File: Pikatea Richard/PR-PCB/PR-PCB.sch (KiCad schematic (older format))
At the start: 7 parts, among them SW1 Rotary_Encoder_Switch, SW2 Rotary_Encoder_Switch

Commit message: updated footprints added gerbers
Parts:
- added U1: ProMicro, promicro:ProMicro, symbol promicro:ProMicro
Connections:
- net at MX2.1 (COL): now also MX1.1 (COL), MX3.1 (COL), MX4.1 (COL), MX5.1 (COL), U1.17 (F7)
- net at MX2.2 (ROW): now also U1.11 (B4)
- net at MX3.2 (ROW): now also U1.10 (E6)
- net at MX4.2 (ROW): now also U1.9 (D7)
- net at MX5.2 (ROW): now also U1.8 (C6)
- net at MX1.2 (ROW): now also U1.12 (B5)
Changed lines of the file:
@@
 	1    0    0    -1
 $EndComp
+$Comp
+L promicro:ProMicro U1
+U 1 1 60242502
+P 4750 4050
+F 0 "U1" H 4750 5087 60  0000 C CNN
+F 1 "ProMicro" H 4750 4981 60  0000 C CNN
+F 2 "promicro:ProMicro" H 4850 3000 60  0001 C CNN
+F 3 "" H 4850 3000 60  0000 C CNN
+	1    4750 4050
+	1    0    0    -1
+$EndComp
+Wire Wire Line
+	4550 2350 4550 2750
+Wire Wire Line
+	4550 2750 4950 2750
+Wire Wire Line
+	4950 2750 4950 2350
+Wire Wire Line
+	4950 2750 5350 2750
+Wire Wire Line
+	5350 2750 5350 2350
+Connection ~ 4950 2750
+Wire Wire Line
+	5350 2750 5750 2750
+Wire Wire Line
+	5750 2750 5750 2350
+Connection ~ 5350 2750
+Wire Wire Line
+	5750 2750 6150 2750
+Wire Wire Line
+	6150 2750 6150 2350
+Connection ~ 5750 2750
+Wire Wire Line
+	6150 2750 6150 4000
+Wire Wire Line
+	6150 4000 5450 4000
+Connection ~ 6150 2750
+Wire Wire Line
+	4350 2550 4350 3050
+Wire Wire Line
+	4350 3050 3900 3050
+Wire Wire Line
+	3900 3050 3900 4400
+Wire Wire Line
+	3900 4400 4050 4400
+Wire Wire Line
+	4050 4300 3950 4300
+Wire Wire Line
+	3950 4300 3950 3100
+Wire Wire Line
+	3950 3100 4750 3100
+Wire Wire Line
+	4750 3100 4750 2550
+Wire Wire Line
+	4050 4200 3650 4200
+Wire Wire Line
+	3650 4200 3650 2950
+Wire Wire Line
+	3650 2950 5150 2950
+Wire Wire Line
+	5150 2950 5150 2550
+Wire Wire Line
+	4050 4100 3750 4100
+Wire Wire Line
+	3750 4100 3750 3000
+Wire Wire Line
+	3750 3000 5550 3000
+Wire Wire Line
+	5550 3000 5550 2550
+Wire Wire Line
+	5950 2550 5950 2900
+Wire Wire Line
+	5950 2900 3800 2900
+Wire Wire Line
+	3800 2900 3800 4000
+Wire Wire Line
+	3800 4000 4050 4000
 $EndSCHEMATC

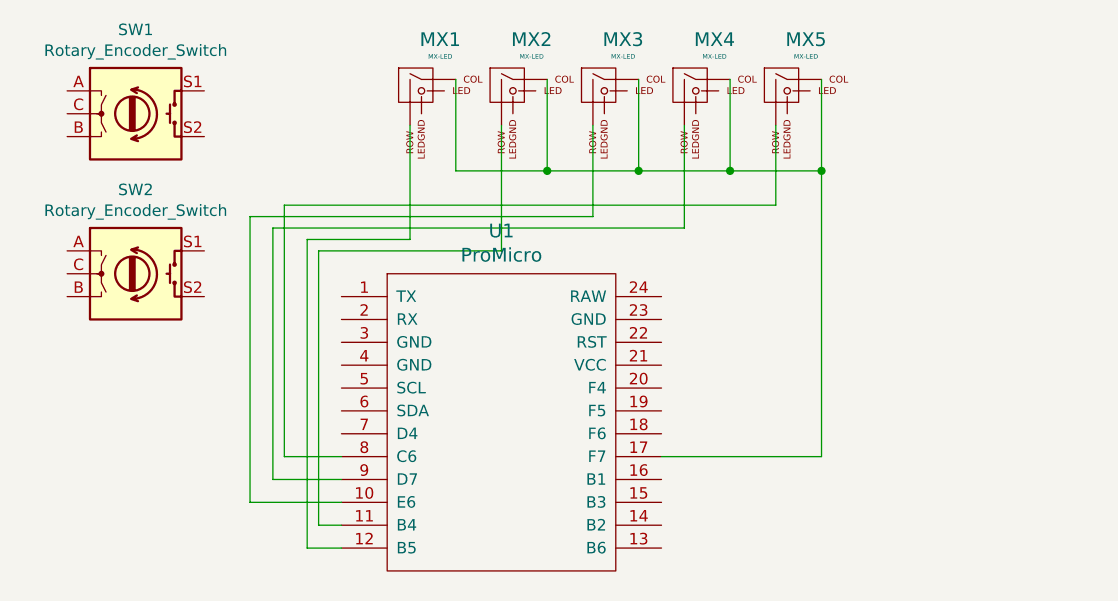
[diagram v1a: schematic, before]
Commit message: update gb4 to kicad 6, add gb4 fkvarient
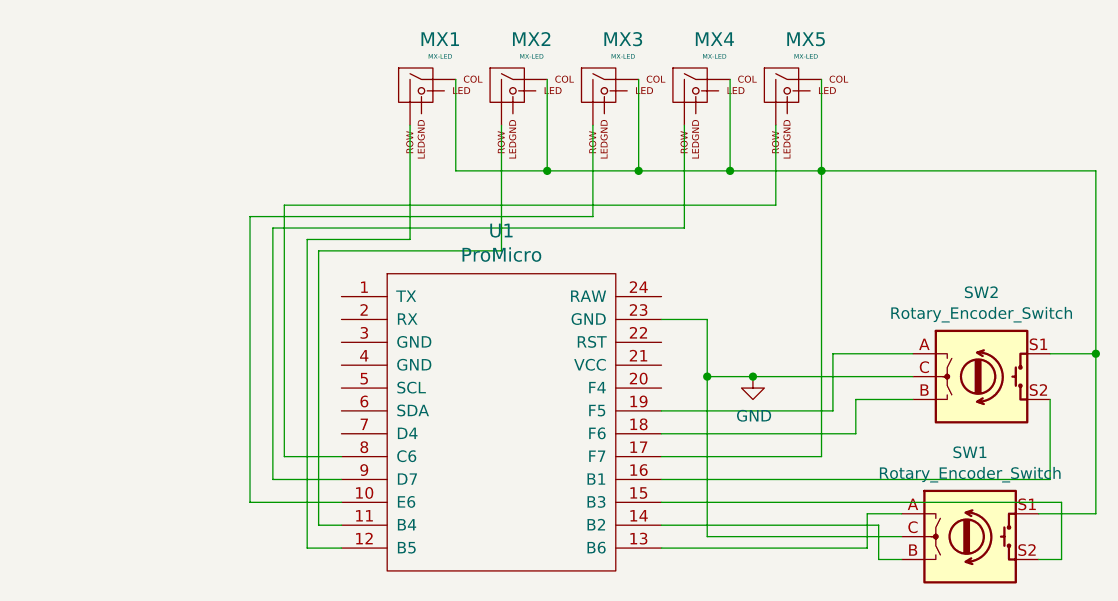
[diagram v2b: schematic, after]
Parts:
- MX1, MX2, MX3, MX4, MX5: footprint MX_Only:MXOnly-1U-Hotswap-Antishear -> MX_Only:MXOnly-1U-NoLED
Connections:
- net at MX1.1 (COL), MX2.1 (COL), MX3.1 (COL)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: now also SW1.S1, SW2.S1
- net at SW1.A: now also U1.13 (B6)
- net at SW1.B: now also U1.14 (B2)
- net GND: now reaches SW1.C
- net GND: now also SW2.C, U1.23 (GND)
- net at SW1.S2: now also U1.15 (B3)
- net at SW2.A: now also U1.19 (F5)
- net at SW2.B: now also U1.18 (F6)
- net at SW2.S2: now also U1.16 (B1)
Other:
- moved on the sheet: SW1, SW2
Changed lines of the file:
@@
 F 0 "MX2" H 4882 2624 60  0000 C CNN
 F 1 "MX-LED" H 4882 2550 20  0000 C CNN
-F 2 "MX_Only:MXOnly-1U-Hotswap-Antishear" H 4175 2375 60  0001 C CNN
+F 2 "MX_Only:MXOnly-1U-NoLED" H 4175 2375 60  0001 C CNN
 F 3 "" H 4175 2375 60  0001 C CNN
 	1    4800 2400
@@
 F 0 "MX3" H 5282 2624 60  0000 C CNN
 F 1 "MX-LED" H 5282 2550 20  0000 C CNN
-F 2 "MX_Only:MXOnly-1U-Hotswap-Antishear" H 4575 2375 60  0001 C CNN
+F 2 "MX_Only:MXOnly-1U-NoLED" H 4575 2375 60  0001 C CNN
 F 3 "" H 4575 2375 60  0001 C CNN
 	1    5200 2400
@@
 F 0 "MX4" H 5682 2624 60  0000 C CNN
 F 1 "MX-LED" H 5682 2550 20  0000 C CNN
-F 2 "MX_Only:MXOnly-1U-Hotswap-Antishear" H 4975 2375 60  0001 C CNN
+F 2 "MX_Only:MXOnly-1U-NoLED" H 4975 2375 60  0001 C CNN
 F 3 "" H 4975 2375 60  0001 C CNN
 	1    5600 2400
@@
 F 0 "MX5" H 6082 2624 60  0000 C CNN
 F 1 "MX-LED" H 6082 2550 20  0000 C CNN
-F 2 "MX_Only:MXOnly-1U-Hotswap-Antishear" H 5375 2375 60  0001 C CNN
+F 2 "MX_Only:MXOnly-1U-NoLED" H 5375 2375 60  0001 C CNN
 F 3 "" H 5375 2375 60  0001 C CNN
 	1    6000 2400
@@
 F 0 "MX1" H 4482 2624 60  0000 C CNN
 F 1 "MX-LED" H 4482 2550 20  0000 C CNN
-F 2 "MX_Only:MXOnly-1U-Hotswap-Antishear" H 3775 2375 60  0001 C CNN
+F 2 "MX_Only:MXOnly-1U-NoLED" H 3775 2375 60  0001 C CNN
 F 3 "" H 3775 2375 60  0001 C CNN
 	1    4400 2400
@@
 L Device:Rotary_Encoder_Switch SW1
 U 1 1 601C8410
-P 3150 2500
-F 0 "SW1" H 3150 2867 50  0000 C CNN
-F 1 "Rotary_Encoder_Switch" H 3150 2776 50  0000 C CNN
-F 2 "Pikatea Macropad Encoder Side Mount:Encoder-BI_EN11_HSM0E" H 3000 2660 50  0001 C CNN
-F 3 "~" H 3150 2760 50  0001 C CNN
-	1    3150 2500
+P 6800 4350
+F 0 "SW1" H 6800 4717 50  0000 C CNN
+F 1 "Rotary_Encoder_Switch" H 6800 4626 50  0000 C CNN
+F 2 "Pikatea Macropad Encoder Side Mount:Encoder-BI_EN11_HSM0E" H 6650 4510 50  0001 C CNN
+F 3 "~" H 6800 4610 50  0001 C CNN
+	1    6800 4350
 	1    0    0    -1
 $EndComp
@@
 L Device:Rotary_Encoder_Switch SW2
 U 1 1 601C8BAC
-P 3150 3200
-F 0 "SW2" H 3150 3567 50  0000 C CNN
-F 1 "Rotary_Encoder_Switch" H 3150 3476 50  0000 C CNN
-F 2 "Pikatea Macropad Encoder Side Mount:Encoder-BI_EN11_HSM0E" H 3000 3360 50  0001 C CNN
-F 3 "~" H 3150 3460 50  0001 C CNN
-	1    3150 3200
+P 6850 3650
+F 0 "SW2" H 6850 4017 50  0000 C CNN
+F 1 "Rotary_Encoder_Switch" H 6850 3926 50  0000 C CNN
+F 2 "Pikatea Macropad Encoder Side Mount:Encoder-BI_EN11_HSM0E" H 6700 3810 50  0001 C CNN
+F 3 "~" H 6850 3910 50  0001 C CNN
+	1    6850 3650
 	1    0    0    -1
 $EndComp
@@
 Wire Wire Line
 	6150 2750 6150 4000
+Connection ~ 6150 2750
+Wire Wire Line
+	4350 2550 4350 3050
+Wire Wire Line
+	4350 3050 3900 3050
+Wire Wire Line
+	3900 3050 3900 4400
+Wire Wire Line
+	3900 4400 4050 4400
+Wire Wire Line
+	4050 4300 3950 4300
+Wire Wire Line
+	3950 4300 3950 3100
+Wire Wire Line
+	3950 3100 4750 3100
+Wire Wire Line
+	4750 3100 4750 2550
+Wire Wire Line
+	4050 4200 3650 4200
+Wire Wire Line
+	3650 4200 3650 2950
+Wire Wire Line
+	3650 2950 5150 2950
+Wire Wire Line
+	5150 2950 5150 2550
+Wire Wire Line
+	4050 4100 3750 4100
+Wire Wire Line
+	3750 4100 3750 3000
+Wire Wire Line
+	3750 3000 5550 3000
+Wire Wire Line
+	5550 3000 5550 2550
+Wire Wire Line
+	5950 2550 5950 2900
+Wire Wire Line
+	5950 2900 3800 2900
+Wire Wire Line
+	3800 2900 3800 4000
+Wire Wire Line
+	3800 4000 4050 4000
+Wire Wire Line
+	6550 3550 6200 3550
+Wire Wire Line
+	6300 3750 6550 3750
+Wire Wire Line
+	6550 3650 5850 3650
+Wire Wire Line
+	5650 3650 5650 3400
+Wire Wire Line
+	5650 3400 5450 3400
+Wire Wire Line
+	6500 4350 5650 4350
+Wire Wire Line
+	5650 4350 5650 3650
+Connection ~ 5650 3650
+Wire Wire Line
+	6400 4300 6400 4450
+Wire Wire Line
+	6400 4450 6500 4450
+Wire Wire Line
+	5450 4300 6400 4300
+Wire Wire Line
+	6350 4400 6350 4250
+Wire Wire Line
+	6350 4250 6500 4250
+Wire Wire Line
+	5450 4400 6350 4400
+$Comp
+L power:GND #PWR0101
+U 1 1 6243C54E
+P 5850 3650
+F 0 "#PWR0101" H 5850 3400 50  0001 C CNN
+F 1 "GND" H 5855 3477 50  0000 C CNN
+F 2 "" H 5850 3650 50  0001 C CNN
+F 3 "" H 5850 3650 50  0001 C CNN
+	1    5850 3650
+	1    0    0    -1
+$EndComp
+Connection ~ 5850 3650
+Wire Wire Line
+	5850 3650 5650 3650
+Wire Wire Line
+	6150 2750 7350 2750
+Wire Wire Line
+	7350 2750 7350 3550
+Wire Wire Line
+	7350 3550 7150 3550
+Wire Wire Line
+	7350 3550 7350 4250
+Wire Wire Line
+	7350 4250 7100 4250
+Connection ~ 7350 3550
 Wire Wire Line
 	6150 4000 5450 4000
-Connection ~ 6150 2750
-Wire Wire Line
-	4350 2550 4350 3050
-Wire Wire Line
-	4350 3050 3900 3050
-Wire Wire Line
-	3900 3050 3900 4400
-Wire Wire Line
-	3900 4400 4050 4400
-Wire Wire Line
-	4050 4300 3950 4300
-Wire Wire Line
-	3950 4300 3950 3100
-Wire Wire Line
-	3950 3100 4750 3100
-Wire Wire Line
-	4750 3100 4750 2550
-Wire Wire Line
-	4050 4200 3650 4200
-Wire Wire Line
-	3650 4200 3650 2950
-Wire Wire Line
-	3650 2950 5150 2950
-Wire Wire Line
-	5150 2950 5150 2550
-Wire Wire Line
-	4050 4100 3750 4100
-Wire Wire Line
-	3750 4100 3750 3000
-Wire Wire Line
-	3750 3000 5550 3000
-Wire Wire Line
-	5550 3000 5550 2550
-Wire Wire Line
-	5950 2550 5950 2900
-Wire Wire Line
-	5950 2900 3800 2900
-Wire Wire Line
-	3800 2900 3800 4000
-Wire Wire Line
-	3800 4000 4050 4000
+Wire Wire Line
+	6200 3550 6200 3800
+Wire Wire Line
+	6200 3800 5450 3800
+Wire Wire Line
+	6300 3900 5450 3900
+Wire Wire Line
+	6300 3900 6300 3750
+Wire Wire Line
+	7150 3750 7150 4100
+Wire Wire Line
+	7150 4100 5450 4100
+Wire Wire Line
+	5450 4200 7200 4200
+Wire Wire Line
+	7200 4200 7200 4450
+Wire Wire Line
+	7200 4450 7100 4450
 $EndSCHEMATC
